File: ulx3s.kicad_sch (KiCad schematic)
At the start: 4 parts

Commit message: start to normalize bom
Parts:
- H1, H2, H3, H4: now left out of the parts list
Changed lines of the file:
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@@
 		(unit 1)
 		(exclude_from_sim no)
-		(in_bom yes)
+		(in_bom no)
 		(on_board yes)
 		(dnp no)
@@
 		(unit 1)
 		(exclude_from_sim no)
-		(in_bom yes)
+		(in_bom no)
 		(on_board yes)
 		(dnp no)
@@
 		(unit 1)
 		(exclude_from_sim no)
-		(in_bom yes)
+		(in_bom no)
 		(on_board yes)
 		(dnp no)
@@
 		(unit 1)
 		(exclude_from_sim no)
-		(in_bom yes)
+		(in_bom no)
 		(on_board yes)
 		(dnp no)

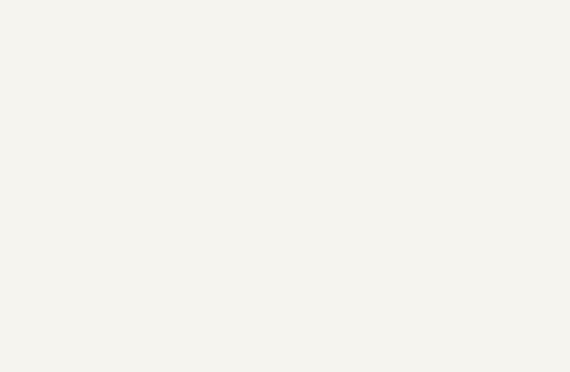
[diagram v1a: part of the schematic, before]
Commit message: updating part numbers across schematcs
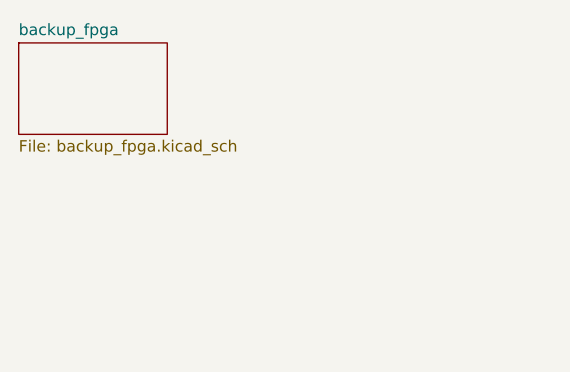
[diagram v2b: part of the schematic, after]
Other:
- added sheet backup_fpga (backup_fpga.kicad_sch)
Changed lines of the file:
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@@
+		)
+	)
+	(sheet
+		(at 55.88 43.18)
+		(size 16.51 10.16)
+		(exclude_from_sim no)
+		(in_bom yes)
+		(on_board yes)
+		(dnp no)
+		(fields_autoplaced yes)
+		(stroke
+			(width 0.1524)
+			(type solid)
+		)
+		(fill
+			(color 0 0 0 0.0000)
+		)
+		(property "Sheetname" "backup_fpga"
+			(at 55.88 42.4684 0)
+			(effects
+				(font
+					(size 1.27 1.27)
+				)
+				(justify left bottom)
+			)
+		)
+		(property "Sheetfile" "backup_fpga.kicad_sch"
+			(at 55.88 53.9246 0)
+			(effects
+				(font
+					(size 1.27 1.27)
+				)
+				(justify left top)
+			)
+		)
+		(instances
+			(project "ulx3s"
+				(path "/49a43414-f3c1-43b2-ad20-ac3166075f21"
+					(page "12")
+				)
+			)
 		)
 	)

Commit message: initial s3 stuff
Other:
- added sheet esp32_s3_wifi (esp32_s3_wifi.kicad_sch)
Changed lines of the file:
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@@
+		)
+	)
+	(sheet
+		(at 102.87 93.98)
+		(size 27.94 21.59)
+		(exclude_from_sim no)
+		(in_bom yes)
+		(on_board yes)
+		(dnp no)
+		(fields_autoplaced yes)
+		(stroke
+			(width 0.1524)
+			(type solid)
+		)
+		(fill
+			(color 0 0 0 0.0000)
+		)
+		(property "Sheetname" "esp32_s3_wifi"
+			(at 102.87 93.2684 0)
+			(effects
+				(font
+					(size 1.27 1.27)
+				)
+				(justify left bottom)
+			)
+		)
+		(property "Sheetfile" "esp32_s3_wifi.kicad_sch"
+			(at 102.87 116.1546 0)
+			(effects
+				(font
+					(size 1.27 1.27)
+				)
+				(justify left top)
+			)
+		)
+		(instances
+			(project "ulx3s"
+				(path "/49a43414-f3c1-43b2-ad20-ac3166075f21"
+					(page "13")
+				)
+			)
 		)
 	)

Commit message: Remove 'Leave Empty' in favor of using attributes
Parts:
- H1, H2, H3: now not fitted
- H4: Note Leave empty -> (none); now not fitted
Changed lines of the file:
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@@
+		)
+	)
+	(text_box "0.0.6 - build\ncurrent\n	- Marked RV2 as DNP - Stencil Issue\n	- VJ1/RP1/RP2/RP3/J1/J2/D51/D52/D9/J4/J6/H1/H2/H3/H4 marked as DNP - doesn't affect stencil"
+		(exclude_from_sim no)
+		(at 153.67 57.15 0)
+		(size 76.2 35.56)
+		(margins 0.9525 0.9525 0.9525 0.9525)
+		(stroke
+			(width 0)
+			(type solid)
+		)
+		(fill
+			(type none)
+		)
+		(effects
+			(font
+				(size 1.524 1.524)
+			)
+			(justify left top)
 		)
 	)
@@
 		(in_bom no)
 		(on_board yes)
-		(in_pos_files yes)
-		(dnp no)
+		(in_pos_files no)
+		(dnp yes)
 		(property "Reference" "H1"
 			(at 77.47 161.29 0)
@@
 		(in_bom no)
 		(on_board yes)
-		(in_pos_files yes)
-		(dnp no)
+		(in_pos_files no)
+		(dnp yes)
 		(property "Reference" "H2"
 			(at 105.41 161.29 0)
@@
 		(in_bom no)
 		(on_board yes)
-		(in_pos_files yes)
-		(dnp no)
+		(in_pos_files no)
+		(dnp yes)
 		(property "Reference" "H3"
 			(at 105.41 143.51 0)
@@
 		(in_bom no)
 		(on_board yes)
-		(in_pos_files yes)
-		(dnp no)
+		(in_pos_files no)
+		(dnp yes)
 		(property "Reference" "H4"
 			(at 77.47 143.51 0)
@@
 			)
 		)
-		(property "Note" "Leave empty"
+		(property "Note" ""
 			(at 80.01 143.51 0)
 			(hide yes)

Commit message: add 0ohm resistor to bom for RV3
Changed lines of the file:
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@@
 		)
 	)
-	(text_box "0.0.6 - build\ncurrent\n	- Marked RV2 as DNP - Stencil Issue\n	- VJ1/RP1/RP2/RP3/J1/J2/D51/D52/D9/J4/J6/H1/H2/H3/H4 marked as DNP - doesn't affect stencil"
+	(text_box "0.0.6 - build\ncurrent\n	- Marked RV2 as DNP - Stencil Issue\n	- VJ1/RP1/RP2/RP3/J1/J2/D51/D52/D9/J4/J6/H1/H2/H3/H4 marked as DNP - doesn't affect stencil\n	- Missing RV3 0ohm resistor"
 		(exclude_from_sim no)
 		(at 153.67 57.15 0)

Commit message: remove analog schematic
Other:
- removed sheet analog
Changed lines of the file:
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@@
-	)
-	(sheet
-		(at 220.98 149.86)
-		(size 19.05 11.43)
-		(exclude_from_sim no)
-		(in_bom yes)
-		(on_board yes)
-		(dnp no)
-		(fields_autoplaced yes)
-		(stroke
-			(width 0)
-			(type solid)
-		)
-		(fill
-			(color 0 0 0 0)
-		)
-		(property "Sheetname" "analog"
-			(at 220.98 149.0214 0)
-			(show_name no)
-			(do_not_autoplace no)
-			(effects
-				(font
-					(size 1.524 1.524)
-				)
-				(justify left bottom)
-			)
-		)
-		(property "Sheetfile" "analog.kicad_sch"
-			(at 220.98 161.9762 0)
-			(show_name no)
-			(do_not_autoplace no)
-			(effects
-				(font
-					(size 1.524 1.524)
-				)
-				(justify left top)
-			)
-		)
-		(instances
-			(project "ulx3s"
-				(path "/49a43414-f3c1-43b2-ad20-ac3166075f21"
-					(page "7")
-				)
-			)
-		)
 	)
 	(sheet
